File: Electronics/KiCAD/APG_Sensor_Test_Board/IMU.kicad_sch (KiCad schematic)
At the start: 0 parts

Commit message: sensor schematics
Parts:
- added C1, C4, C5: 0.1uF, symbol Device:C_Small
- added U1: ICM-20948, Sensor_Motion:InvenSense_QFN-24_3x3mm_P0.4mm, symbol Sensor_Motion:ICM-20948
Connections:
- new net: C4.1, U1.10 (REGOUT)
- new net +1V8: C1.1, C5.1, U1.13 (VDD), U1.8 (VDDIO)
- new net FSYNC: U1.11 (FSYNC)
- new net GND: C1.2, C4.2, C5.2, U1.18 (GND), U1.20 (GND)
- new net INT1: U1.12 (INT1)
- new net SCLK: U1.23 (SCL/SCLK)
- new net SDI: U1.24 (SDA/SDI)
- new net SDO: U1.9 (SDO/AD0)
- new net nCS: U1.22 (~{CS})

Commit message: Gannon inspection decision to change IMU
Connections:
- net FSYNC: no longer names the net of U1.11 (FSYNC)
- net INT1: no longer names the net of U1.12 (INT1)
- net SCLK: no longer names the net of U1.23 (SCL/SCLK)
- net SDI: no longer names the net of U1.24 (SDA/SDI)
- net SDO: no longer names the net of U1.9 (SDO/AD0)
- net nCS: no longer names the net of U1.22 (~{CS})
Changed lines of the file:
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@@
 	(wire
 		(pts
-			(xy 114.3 83.82) (xy 116.84 83.82)
+			(xy 72.39 83.82) (xy 116.84 83.82)
 		)
 		(stroke
@@
 		(pts
 			(xy 137.16 62.23) (xy 137.16 59.69)
-		)
-		(stroke
-			(width 0)
-			(type default)
-		)
-	)
-	(wire
-		(pts
-			(xy 114.3 81.28) (xy 116.84 81.28)
 		)
 		(stroke
@@
 		(pts
 			(xy 121.92 59.69) (xy 127 59.69)
-		)
-		(stroke
-			(width 0)
-			(type default)
-		)
-	)
-	(wire
-		(pts
-			(xy 114.3 93.98) (xy 116.84 93.98)
 		)
 		(stroke
@@
 		(pts
 			(xy 144.78 91.44) (xy 142.24 91.44)
+		)
+		(stroke
+			(width 0)
+			(type default)
+		)
+	)
+	(wire
+		(pts
+			(xy 72.39 93.98) (xy 116.84 93.98)
 		)
 		(stroke
@@
 		)
 	)
-	(hierarchical_label "SDO"
-		(shape input)
-		(at 114.3 78.74 180)
-		(fields_autoplaced yes)
-		(effects
-			(font
-				(size 1.27 1.27)
-			)
-			(justify right)
+	(wire
+		(pts
+			(xy 72.39 81.28) (xy 116.84 81.28)
+		)
+		(stroke
+			(width 0)
+			(type default)
 		)
 	)
-	(hierarchical_label "nCS"
-		(shape input)
-		(at 114.3 86.36 180)
-		(fields_autoplaced yes)
-		(effects
-			(font
-				(size 1.27 1.27)
-			)
-			(justify right)
-		)
-	)
-	(hierarchical_label "SDI"
-		(shape input)
-		(at 114.3 81.28 180)
-		(fields_autoplaced yes)
-		(effects
-			(font
-				(size 1.27 1.27)
-			)
-			(justify right)
-		)
-	)
-	(hierarchical_label "FSYNC"
-		(shape input)
-		(at 114.3 91.44 180)
-		(fields_autoplaced yes)
-		(effects
-			(font
-				(size 1.27 1.27)
-			)
-			(justify right)
-		)
-	)
-	(hierarchical_label "INT1"
-		(shape output)
-		(at 114.3 93.98 180)
-		(fields_autoplaced yes)
-		(effects
-			(font
-				(size 1.27 1.27)
-			)
-			(justify right)
-		)
-	)
-	(hierarchical_label "SCLK"
-		(shape input)
-		(at 114.3 83.82 180)
-		(fields_autoplaced yes)
-		(effects
-			(font
-				(size 1.27 1.27)
-			)
-			(justify right)
-		)
-	)

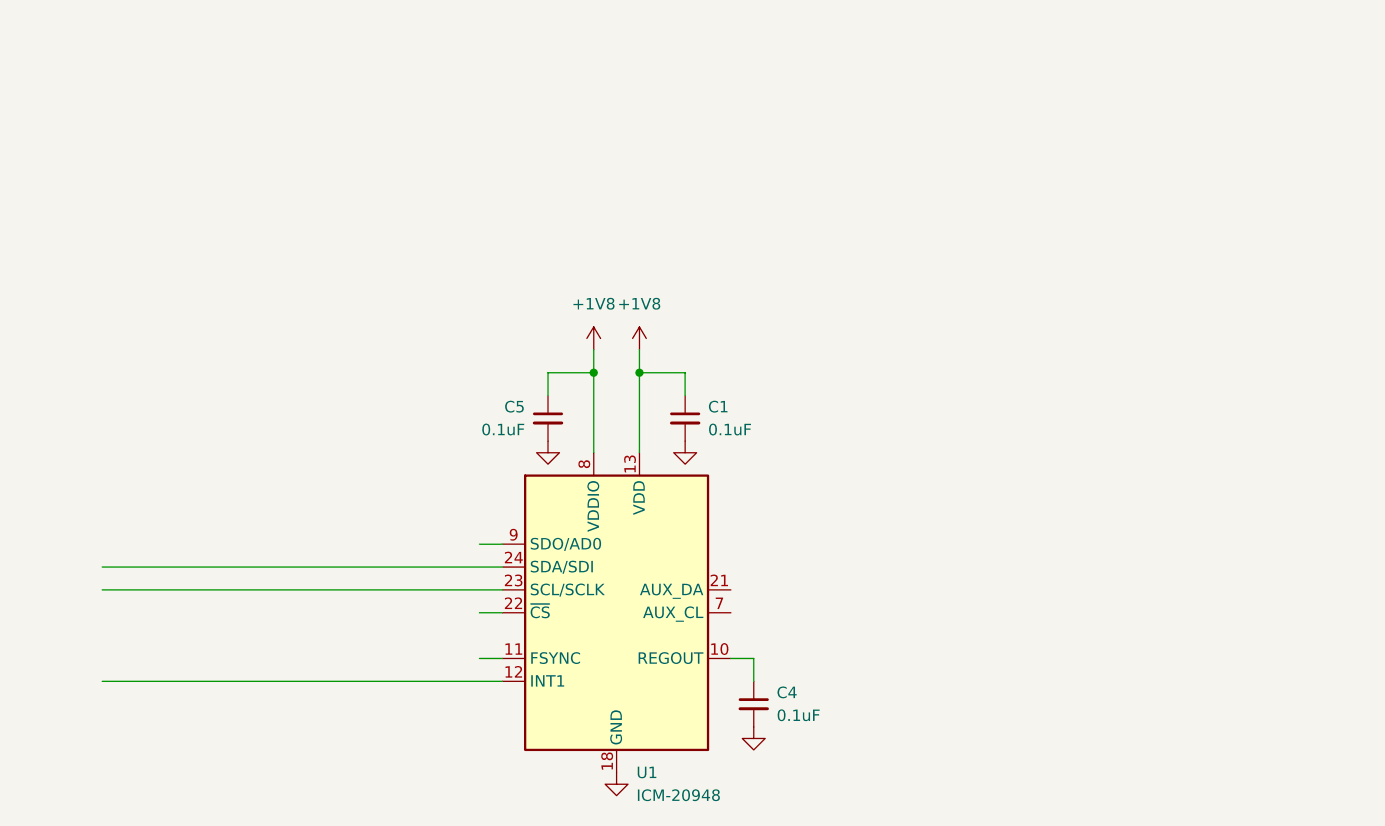
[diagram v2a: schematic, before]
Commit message: Changed IMU and changed sensors to I2C
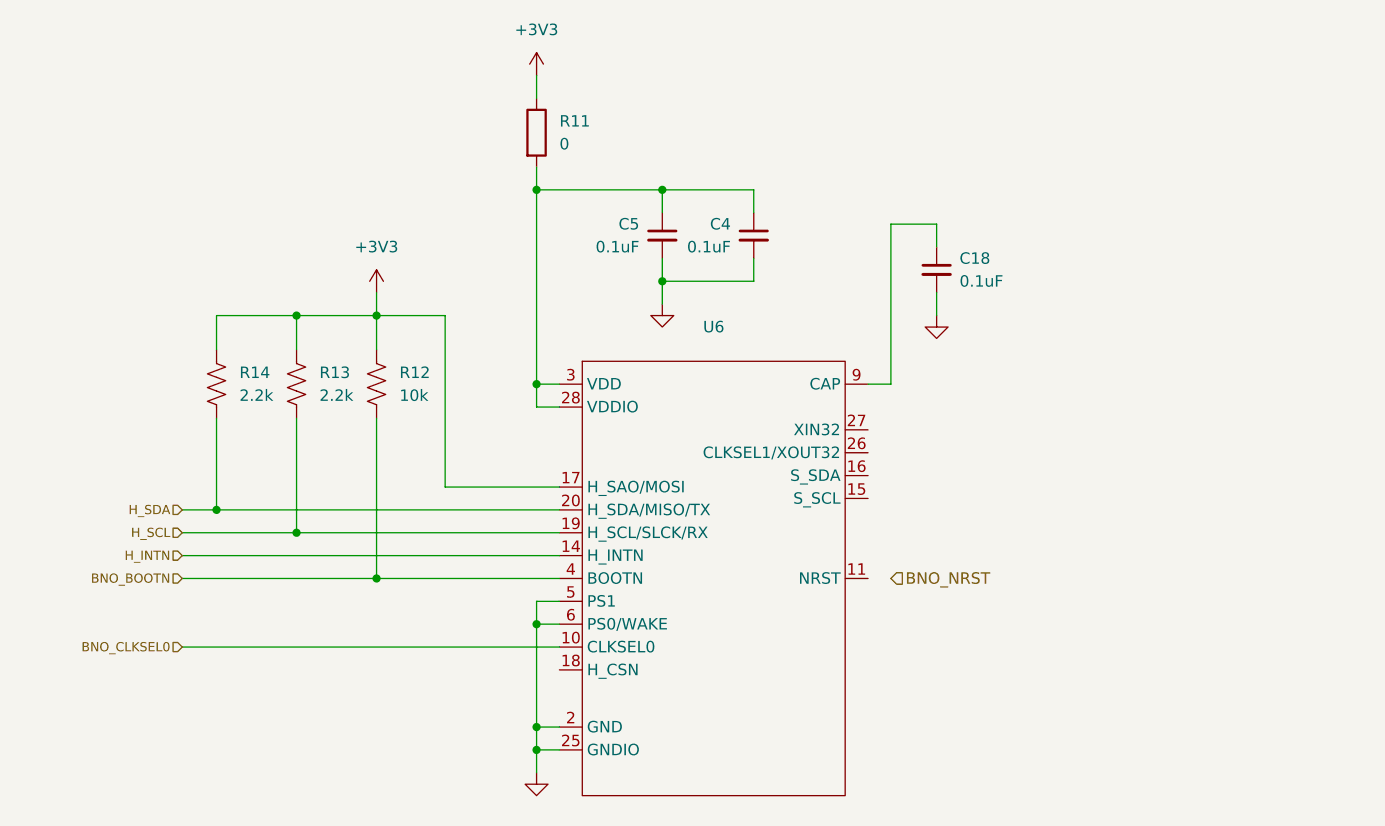
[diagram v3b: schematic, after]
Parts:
- removed C1: 0.1uF, symbol Device:C_Small
- removed U1: ICM-20948, Sensor_Motion:InvenSense_QFN-24_3x3mm_P0.4mm, symbol Sensor_Motion:ICM-20948
- added C18: 0.1uF, symbol Device:C_Small
- added R11: 0, symbol Device:R
- added R12: 10k, symbol Device:R_US
- added R13, R14: 2.2k, symbol Device:R_US
- added U6: ~, symbol Project:BNO086
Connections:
- net +1V8 is gone; now on an unnamed net: C5.1
- net GND: now also C18.2, U6.2 (GND), U6.25 (GNDIO), U6.5 (PS1), U6.6 (PS0/WAKE)
- net at C4.1: now also R11.2, U6.28 (VDDIO), U6.3 (VDD)
- new net: C18.1, U6.9 (CAP)
- new net +3V3: R11.1, R12.1, R13.1, R14.1, U6.17 (H_SAO/MOSI)
- new net BNO_BOOTN: R12.2, U6.4 (BOOTN)
- new net BNO_CLKSEL0: U6.10 (CLKSEL0)
- new net H_INTN: U6.14 (H_INTN)
- new net H_SCL: R13.2, U6.19 (H_SCL/SLCK/RX)
- new net H_SDA: R14.2, U6.20 (H_SDA/MISO/TX)
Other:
- moved on the sheet: C5

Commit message: Main Schematic Complete
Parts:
- removed R13, R14: 2.2k, symbol Device:R_US
- U6: value ~ -> BNO085
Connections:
- net BNO_CLKSEL0 is gone; now on net +3V3: U6.10 (CLKSEL0)
- net BNO_NRST: now also U6.11 (NRST)
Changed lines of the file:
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@@
-	)
-	(junction
-		(at 93.98 77.47)
-		(diameter 0)
-		(color 0 0 0 0)
-	)
-	(junction
-		(at 85.09 74.93)
-		(diameter 0)
-		(color 0 0 0 0)
 	)
 	(junction
@@
 	)
 	(junction
-		(at 93.98 53.34)
-		(diameter 0)
-		(color 0 0 0 0)
-	)
-	(junction
 		(at 120.65 60.96)
 		(diameter 0)
@@
 	(wire
 		(pts
+			(xy 116.84 90.17) (xy 123.19 90.17)
+		)
+		(stroke
+			(width 0)
+			(type default)
+		)
+	)
+	(wire
+		(pts
 			(xy 160.02 43.18) (xy 165.1 43.18)
 		)
@@
 	(wire
 		(pts
-			(xy 85.09 74.93) (xy 123.19 74.93)
-		)
-		(stroke
-			(width 0)
-			(type default)
-		)
-	)
-	(wire
-		(pts
 			(xy 160.02 60.96) (xy 160.02 43.18)
 		)
@@
 	(wire
 		(pts
-			(xy 93.98 64.77) (xy 93.98 77.47)
-		)
-		(stroke
-			(width 0)
-			(type default)
-		)
-	)
-	(wire
-		(pts
 			(xy 165.1 50.8) (xy 165.1 53.34)
 		)
@@
 	(wire
 		(pts
-			(xy 93.98 53.34) (xy 102.87 53.34)
-		)
-		(stroke
-			(width 0)
-			(type default)
-		)
-	)
-	(wire
-		(pts
 			(xy 144.78 49.53) (xy 144.78 46.99)
 		)
@@
 	(wire
 		(pts
-			(xy 85.09 57.15) (xy 85.09 53.34)
-		)
-		(stroke
-			(width 0)
-			(type default)
-		)
-	)
-	(wire
-		(pts
 			(xy 110.49 53.34) (xy 102.87 53.34)
 		)
@@
 	(wire
 		(pts
-			(xy 85.09 64.77) (xy 85.09 74.93)
-		)
-		(stroke
-			(width 0)
-			(type default)
-		)
-	)
-	(wire
-		(pts
 			(xy 81.28 82.55) (xy 102.87 82.55)
 		)
@@
 	(wire
 		(pts
-			(xy 93.98 77.47) (xy 123.19 77.47)
-		)
-		(stroke
-			(width 0)
-			(type default)
-		)
-	)
-	(wire
-		(pts
-			(xy 81.28 90.17) (xy 123.19 90.17)
+			(xy 81.28 77.47) (xy 123.19 77.47)
 		)
 		(stroke
@@
 	(wire
 		(pts
+			(xy 157.48 82.55) (xy 160.02 82.55)
+		)
+		(stroke
+			(width 0)
+			(type default)
+		)
+	)
+	(wire
+		(pts
 			(xy 134.62 52.07) (xy 134.62 49.53)
 		)
@@
 	(wire
 		(pts
-			(xy 85.09 53.34) (xy 93.98 53.34)
-		)
-		(stroke
-			(width 0)
-			(type default)
-		)
-	)
-	(wire
-		(pts
 			(xy 120.65 87.63) (xy 120.65 99.06)
 		)
@@
 	(wire
 		(pts
-			(xy 81.28 74.93) (xy 85.09 74.93)
+			(xy 81.28 74.93) (xy 123.19 74.93)
 		)
 		(stroke
@@
 		(pts
 			(xy 102.87 50.8) (xy 102.87 53.34)
-		)
-		(stroke
-			(width 0)
-			(type default)
-		)
-	)
-	(wire
-		(pts
-			(xy 93.98 53.34) (xy 93.98 57.15)
-		)
-		(stroke
-			(width 0)
-			(type default)
-		)
-	)
-	(wire
-		(pts
-			(xy 81.28 77.47) (xy 93.98 77.47)
 		)
 		(stroke
@@
 		(shape input)
 		(at 81.28 77.47 180)
-		(fields_autoplaced yes)
-		(effects
-			(font
-				(size 1.016 1.016)
-			)
-			(justify right)
-		)
-	)
-	(hierarchical_label "BNO_CLKSEL0"
-		(shape input)
-		(at 81.28 90.17 180)
 		(fields_autoplaced yes)
 		(effects
@@
 	)
 	(symbol
-		(lib_id "Device:R_US")
-		(at 93.98 60.96 0)
-		(unit 1)
-		(exclude_from_sim no)
-		(in_bom yes)
-		(on_board yes)
-		(dnp no)
-		(fields_autoplaced yes)
-		(property "Reference" "R13"
-			(at 96.52 59.6899 0)
-			(effects
-				(font
-					(size 1.27 1.27)
-				)
-				(justify left)
-			)
-		)
-		(property "Value" "2.2k"
-			(at 96.52 62.2299 0)
-			(effects
-				(font
-					(size 1.27 1.27)
-				)
-				(justify left)
-			)
-		)
-		(property "Footprint" ""
-			(at 94.996 61.214 90)
-			(effects
-				(font
-					(size 1.27 1.27)
-				)
-				(hide yes)
-			)
-		)
-		(property "Datasheet" "~"
-			(at 93.98 60.96 0)
-			(effects
-				(font
-					(size 1.27 1.27)
-				)
-				(hide yes)
-			)
-		)
-		(property "Description" "Resistor, US symbol"
-			(at 93.98 60.96 0)
-			(effects
-				(font
-					(size 1.27 1.27)
-				)
-				(hide yes)
-			)
-		)
-		(pin "1"
-		)
-		(pin "2"
-		)
-		(instances
-			(project "APG_Sensor_Test_Board"
-				(path "/3161be0c-372f-463d-be0a-bab00f344057/f8ef0a61-6d05-44d0-a94d-ca2583f2f5fd"
-					(reference "R13")
-					(unit 1)
-				)
-			)
-		)
-	)
-	(symbol
 		(lib_id "Project:BNO086")
 		(at 121.92 57.15 0)
@@
 			)
 		)
-		(property "Value" "~"
+		(property "Value" "BNO085"
 			(at 140.335 57.15 0)
 			(effects
@@
 				(path "/3161be0c-372f-463d-be0a-bab00f344057/f8ef0a61-6d05-44d0-a94d-ca2583f2f5fd"
 					(reference "R12")
+					(unit 1)
+				)
+			)
+		)
+	)
+	(symbol
+		(lib_id "power:+3V3")
+		(at 116.84 90.17 0)
+		(unit 1)
+		(exclude_from_sim no)
+		(in_bom yes)
+		(on_board yes)
+		(dnp no)
+		(fields_autoplaced yes)
+		(property "Reference" "#PWR016"
+			(at 116.84 93.98 0)
+			(effects
+				(font
+					(size 1.27 1.27)
+				)
+				(hide yes)
+			)
+		)
+		(property "Value" "+3V3"
+			(at 116.84 85.09 0)
+			(effects
+				(font
+					(size 1.27 1.27)
+				)
+			)
+		)
+		(property "Footprint" ""
+			(at 116.84 90.17 0)
+			(effects
+				(font
+					(size 1.27 1.27)
+				)
+				(hide yes)
+			)
+		)
+		(property "Datasheet" ""
+			(at 116.84 90.17 0)
+			(effects
+				(font
+					(size 1.27 1.27)
+				)
+				(hide yes)
+			)
+		)
+		(property "Description" "Power symbol creates a global label with name \"+3V3\""
+			(at 116.84 90.17 0)
+			(effects
+				(font
+					(size 1.27 1.27)
+				)
+				(hide yes)
+			)
+		)
+		(pin "1"
+		)
+		(instances
+			(project "APG_Sensor_Test_Board"
+				(path "/3161be0c-372f-463d-be0a-bab00f344057/f8ef0a61-6d05-44d0-a94d-ca2583f2f5fd"
+					(reference "#PWR016")
 					(unit 1)
 				)
@@
 					(unit 1)
 				)
-			)
-		)
-	)
-	(symbol
-		(lib_id "Device:R_US")
-		(at 85.09 60.96 0)
-		(unit 1)
-		(exclude_from_sim no)
-		(in_bom yes)
-		(on_board yes)
-		(dnp no)
-		(fields_autoplaced yes)
-		(property "Reference" "R14"
-			(at 87.63 59.6899 0)
-			(effects
-				(font
-					(size 1.27 1.27)
-				)
-				(justify left)
-			)
-		)
-		(property "Value" "2.2k"
-			(at 87.63 62.2299 0)
-			(effects
-				(font
-					(size 1.27 1.27)
-				)
-				(justify left)
-			)
-		)
-		(property "Footprint" ""
-			(at 86.106 61.214 90)
-			(effects
-				(font
-					(size 1.27 1.27)
-				)
-				(hide yes)
-			)
-		)
-		(property "Datasheet" "~"
-			(at 85.09 60.96 0)
-			(effects
-				(font
-					(size 1.27 1.27)
-				)
-				(hide yes)
-			)
-		)
-		(property "Description" "Resistor, US symbol"
-			(at 85.09 60.96 0)
-			(effects
-				(font
-					(size 1.27 1.27)
-				)
-				(hide yes)
-			)
-		)
-		(pin "1"
-		)
-		(pin "2"
-		)
-		(instances
-			(project "APG_Sensor_Test_Board"
-				(path "/3161be0c-372f-463d-be0a-bab00f344057/f8ef0a61-6d05-44d0-a94d-ca2583f2f5fd"
-					(reference "R14")
-					(unit 1)
-				)

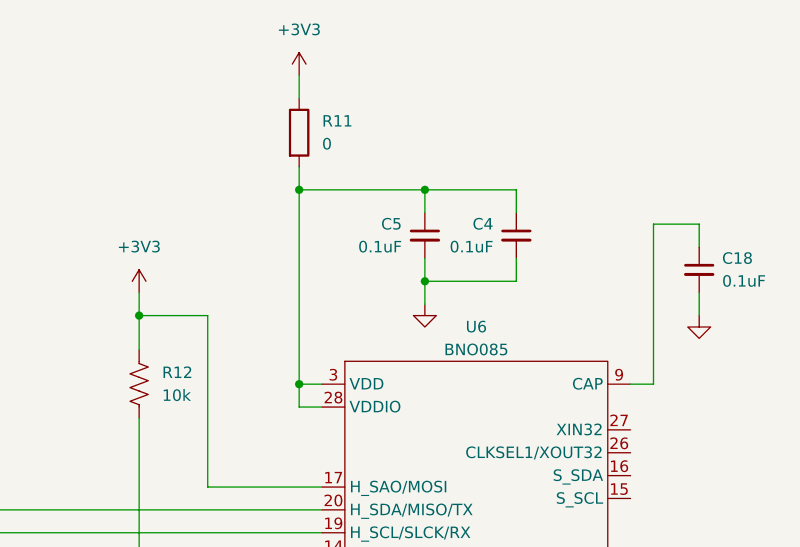
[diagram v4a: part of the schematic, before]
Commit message: reaninotate and begin footprints
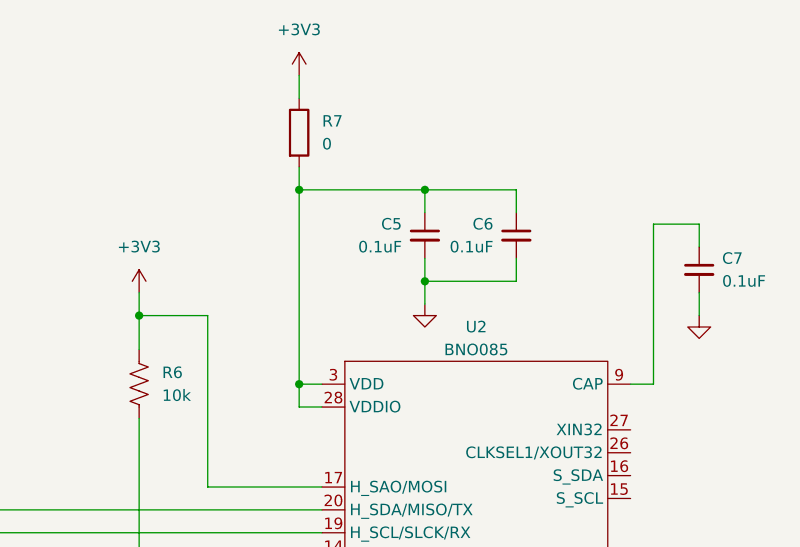
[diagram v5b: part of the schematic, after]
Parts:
- C5: footprint (none) -> Capacitor_SMD:C_0805_2012Metric
- C6: renamed from C4; footprint (none) -> Capacitor_SMD:C_0805_2012Metric
- C7: renamed from C18; footprint (none) -> Capacitor_SMD:C_0805_2012Metric
- R6: renamed from R12; footprint (none) -> Resistor_SMD:R_0805_2012Metric
- R7: renamed from R11; footprint (none) -> Resistor_SMD:R_0805_2012Metric
- renumbered U6 to U2
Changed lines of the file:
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@@
 		(dnp no)
 		(fields_autoplaced yes)
-		(property "Reference" "R11"
+		(property "Reference" "R7"
 			(at 123.19 31.7499 0)
 			(effects
@@
 			)
 		)
-		(property "Footprint" ""
+		(property "Footprint" "Resistor_SMD:R_0805_2012Metric"
 			(at 118.872 33.02 90)
 			(effects
@@
 			(project "APG_Sensor_Test_Board"
 				(path "/3161be0c-372f-463d-be0a-bab00f344057/f8ef0a61-6d05-44d0-a94d-ca2583f2f5fd"
-					(reference "R11")
+					(reference "R7")
 					(unit 1)
 				)
@@
 		(dnp no)
 		(fields_autoplaced yes)
-		(property "Reference" "#PWR05"
+		(property "Reference" "#PWR018"
 			(at 120.65 110.49 0)
 			(effects
@@
 			(project ""
 				(path "/3161be0c-372f-463d-be0a-bab00f344057/f8ef0a61-6d05-44d0-a94d-ca2583f2f5fd"
-					(reference "#PWR05")
+					(reference "#PWR018")
 					(unit 1)
 				)
@@
 		(dnp no)
 		(fields_autoplaced yes)
-		(property "Reference" "U6"
+		(property "Reference" "U2"
 			(at 140.335 54.61 0)
 			(effects
@@
 			(project ""
 				(path "/3161be0c-372f-463d-be0a-bab00f344057/f8ef0a61-6d05-44d0-a94d-ca2583f2f5fd"
-					(reference "U6")
+					(reference "U2")
 					(unit 1)
 				)
@@
 		(dnp no)
 		(fields_autoplaced yes)
-		(property "Reference" "#PWR07"
+		(property "Reference" "#PWR017"
 			(at 120.65 30.48 0)
 			(effects
@@
 			(project ""
 				(path "/3161be0c-372f-463d-be0a-bab00f344057/f8ef0a61-6d05-44d0-a94d-ca2583f2f5fd"
-					(reference "#PWR07")
+					(reference "#PWR017")
 					(unit 1)
 				)
@@
 		(dnp no)
 		(fields_autoplaced yes)
-		(property "Reference" "R12"
+		(property "Reference" "R6"
 			(at 105.41 59.6899 0)
 			(effects
@@
 			)
 		)
-		(property "Footprint" ""
+		(property "Footprint" "Resistor_SMD:R_0805_2012Metric"
 			(at 103.886 61.214 90)
 			(effects
@@
 			(project "APG_Sensor_Test_Board"
 				(path "/3161be0c-372f-463d-be0a-bab00f344057/f8ef0a61-6d05-44d0-a94d-ca2583f2f5fd"
-					(reference "R12")
+					(reference "R6")
 					(unit 1)
 				)
@@
 		(dnp no)
 		(fields_autoplaced yes)
-		(property "Reference" "C4"
+		(property "Reference" "C6"
 			(at 142.24 43.1862 0)
 			(effects
@@
 			)
 		)
-		(property "Footprint" ""
+		(property "Footprint" "Capacitor_SMD:C_0805_2012Metric"
 			(at 144.78 44.45 0)
 			(effects
@@
 			(project "APG_Sensor_Test_Board"
 				(path "/3161be0c-372f-463d-be0a-bab00f344057/f8ef0a61-6d05-44d0-a94d-ca2583f2f5fd"
-					(reference "C4")
+					(reference "C6")
 					(unit 1)
 				)
@@
 		(dnp no)
 		(fields_autoplaced yes)
-		(property "Reference" "#PWR06"
+		(property "Reference" "#PWR020"
 			(at 165.1 59.69 0)
 			(effects
@@
 			(project "APG_Sensor_Test_Board"
 				(path "/3161be0c-372f-463d-be0a-bab00f344057/f8ef0a61-6d05-44d0-a94d-ca2583f2f5fd"
-					(reference "#PWR06")
+					(reference "#PWR020")
 					(unit 1)
 				)
@@
 		(on_board yes)
 		(dnp no)
-		(property "Reference" "C18"
+		(property "Reference" "C7"
 			(at 167.64 46.9962 0)
 			(effects
@@
 			)
 		)
-		(property "Footprint" ""
+		(property "Footprint" "Capacitor_SMD:C_0805_2012Metric"
 			(at 165.1 48.26 0)
 			(effects
@@
 			(project "APG_Sensor_Test_Board"
 				(path "/3161be0c-372f-463d-be0a-bab00f344057/f8ef0a61-6d05-44d0-a94d-ca2583f2f5fd"
-					(reference "C18")
+					(reference "C7")
 					(unit 1)
 				)
@@
 		(dnp no)
 		(fields_autoplaced yes)
-		(property "Reference" "#PWR08"
+		(property "Reference" "#PWR019"
 			(at 134.62 58.42 0)
 			(effects
@@
 			(project "APG_Sensor_Test_Board"
 				(path "/3161be0c-372f-463d-be0a-bab00f344057/f8ef0a61-6d05-44d0-a94d-ca2583f2f5fd"
-					(reference "#PWR08")
+					(reference "#PWR019")
 					(unit 1)
 				)
@@
 			)
 		)
-		(property "Footprint" ""
+		(property "Footprint" "Capacitor_SMD:C_0805_2012Metric"
 			(at 134.62 44.45 0)
 			(effects

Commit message: completed footprint assignment
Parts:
- U2: footprint (none) -> Package_LGA:LGA-28_5.2x3.8mm_P0.5mm
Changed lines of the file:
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@@
 			)
 		)
-		(property "Footprint" ""
+		(property "Footprint" "Package_LGA:LGA-28_5.2x3.8mm_P0.5mm"
 			(at 121.92 57.15 0)
 			(effects
@@
 			(at 121.92 57.15 0)
 			(effects
+				(font
+					(size 1.27 1.27)
+				)
+				(hide yes)
+			)
+		)
+		(property "JLCPCB" ""
+			(at 121.92 57.15 0)
+			(effects
